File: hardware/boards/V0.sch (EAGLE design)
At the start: 140 parts, among them IC2 TPS6300, J1 SJ-43515TS-SMT, J2 HIROSE_DM3BT-DSF-PEJSHIROSE_D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, J3 MOLEX_105450-0101MOLEX_105450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, Q2 ON_SEMI_MMBT5551LT1GON_SEMI_M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, U1 VS1053-L, U2 MICROCHIP_MCP73831T-2ATI-OTMI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, X3 FH12-45S-0.5SH

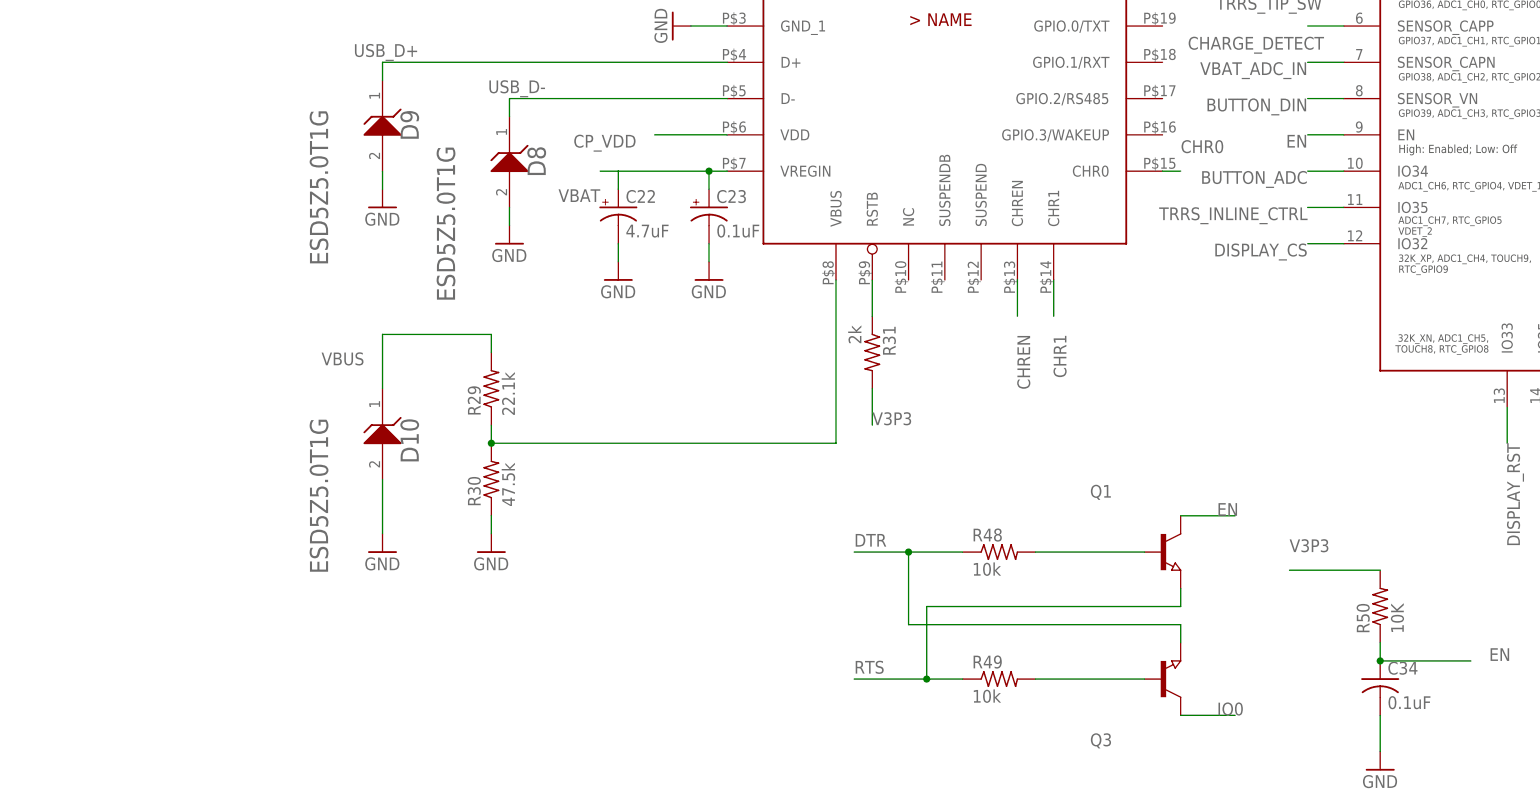
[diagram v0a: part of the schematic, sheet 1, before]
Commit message: checkpoint: swapped resistors for the esp32/cp2102N/usb port, routed the usb port, and swapped the power source for the CP2102N (runs off the 3.3V regulator now; no sense in the device appearing on computers when it isn't powered on - we'll still be able to charge though)
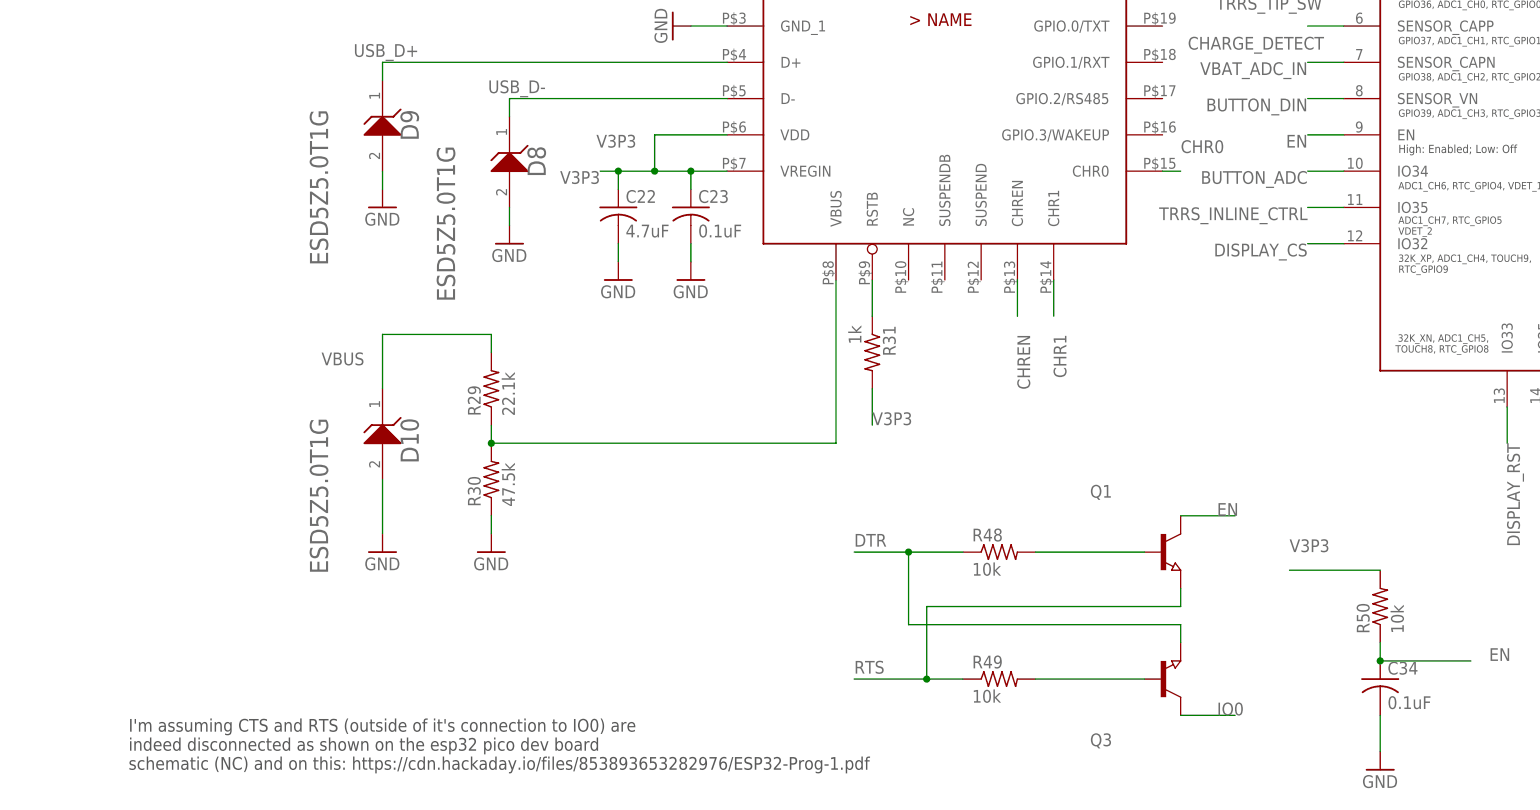
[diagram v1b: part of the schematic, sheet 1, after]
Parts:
- C22, C23: device rcl:CPOL-USC/6032-28R -> rcl:C-USC0402
- C32, C33: device rcl:C-USC1206 -> rcl:C-USC0402
- R27, R28, R29, R30, R46, R47, R48, R49: device rcl:R-US_R0805 -> rcl:R-US_R0402
- R31: value 2k -> 1k; device rcl:R-US_R0805 -> rcl:R-US_R0402
- R50: value 10K -> 10k; device rcl:R-US_R0805 -> rcl:R-US_R0402
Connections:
- net N$53 renamed CP_RSTB
- removed net CP_VDD: JL.VDD
- net GND: now also C22.2, C23.2; no longer C22.-, C23.-
- net V3P3: now also C22.1, C23.1, JL.VDD, JL.VREGIN
- net VBAT: no longer C22.+, C23.+, JL.VREGIN
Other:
- note added: "I'm assuming CTS and RTS (outside of it's connection to IO0) are indeed disconnected as shown on the esp32 pico dev board schematic (NC) and on this: https://cdn.hackaday.io/files/853893653282976/ESP32-Prog-1.pdf"

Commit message: board checkpoint
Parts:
- J12: value SJ-43515TS-SMT -> 3.5mm TRRS Jack
- renumbered J1 to J12
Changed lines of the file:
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@@
 <part name="U$5" library="CR43NP-4R7MC" deviceset="CR43NP-2R2MC" device=""/>
 <part name="BATT_CON" library="JST-S3B-XH-SM4-TB" deviceset="JST_S3B-XH-SM4-TB" device="JST_S3B-XH-SM4-TB_0_0"/>
-<part name="J1" library="TRRS-Jack-SJ-43515TS-SMT" deviceset="SJ-43515TS-SMT" device=""/>
+<part name="J12" library="TRRS-Jack-SJ-43515TS-SMT" deviceset="SJ-43515TS-SMT" device="" value="3.5mm TRRS Jack"/>
 <part name="U$6" library="AT42QT2120" deviceset="COMMS-AT42QT2120" device="XU" package3d_urn="urn:adsk.eagle:package:4349/2" value="COMMS-AT42QT2120XU"/>
 <part name="C1" library="rcl" library_urn="urn:adsk.eagle:library:334" deviceset="C-US" device="C0201" package3d_urn="urn:adsk.eagle:package:23690/2" value="50uF"/>
@@
 </plain>
 <instances>
-<instance part="J1" gate="G$1" x="111.76" y="60.96" smashed="yes" rot="R180">
+<instance part="J12" gate="G$1" x="111.76" y="60.96" smashed="yes" rot="R180">
 <attribute name="NAME" x="119.39685" y="52.55948125" size="1.78193125" layer="95" rot="R180"/>
 <attribute name="VALUE" x="119.40558125" y="71.1542" size="1.78396875" layer="96" rot="R180"/>
@@
 <net name="TRRS_TIP_SW" class="0">
 <segment>
-<pinref part="J1" gate="G$1" pin="TIP_SWITCH"/>
+<pinref part="J12" gate="G$1" pin="TIP_SWITCH"/>
 <wire x1="101.6" y1="63.5" x2="127" y2="63.5" width="0.1524" layer="91"/>
 <label x="129.54" y="63.5" size="1.778" layer="95"/>
@@
 <wire x1="96.52" y1="-5.08" x2="96.52" y2="10.16" width="0.1524" layer="91"/>
 <wire x1="96.52" y1="10.16" x2="127" y2="10.16" width="0.1524" layer="91"/>
-<pinref part="J1" gate="G$1" pin="RING2"/>
+<pinref part="J12" gate="G$1" pin="RING2"/>
 <wire x1="101.6" y1="58.42" x2="96.52" y2="58.42" width="0.1524" layer="91"/>
 <wire x1="96.52" y1="58.42" x2="96.52" y2="48.26" width="0.1524" layer="91"/>
@@
 <wire x1="20.32" y1="-2.54" x2="93.98" y2="-2.54" width="0.1524" layer="91"/>
 <wire x1="93.98" y1="-2.54" x2="93.98" y2="27.94" width="0.1524" layer="91"/>
-<pinref part="J1" gate="G$1" pin="RING1"/>
+<pinref part="J12" gate="G$1" pin="RING1"/>
 <wire x1="101.6" y1="60.96" x2="93.98" y2="60.96" width="0.1524" layer="91"/>
 <wire x1="93.98" y1="60.96" x2="93.98" y2="27.94" width="0.1524" layer="91"/>
@@
 <net name="TRRS_INLINE_CTRL" class="0">
 <segment>
-<pinref part="J1" gate="G$1" pin="SLEEVE"/>
+<pinref part="J12" gate="G$1" pin="SLEEVE"/>
 <wire x1="101.6" y1="55.88" x2="124.46" y2="55.88" width="0.1524" layer="91"/>
 <label x="129.54" y="55.88" size="1.778" layer="95"/>
@@
 <net name="N$57" class="0">
 <segment>
-<pinref part="J1" gate="G$1" pin="TIP"/>
+<pinref part="J12" gate="G$1" pin="TIP"/>
 <wire x1="91.44" y1="66.04" x2="101.6" y2="66.04" width="0.1524" layer="91"/>
 <pinref part="TP3" gate="G$1" pin="TP"/>

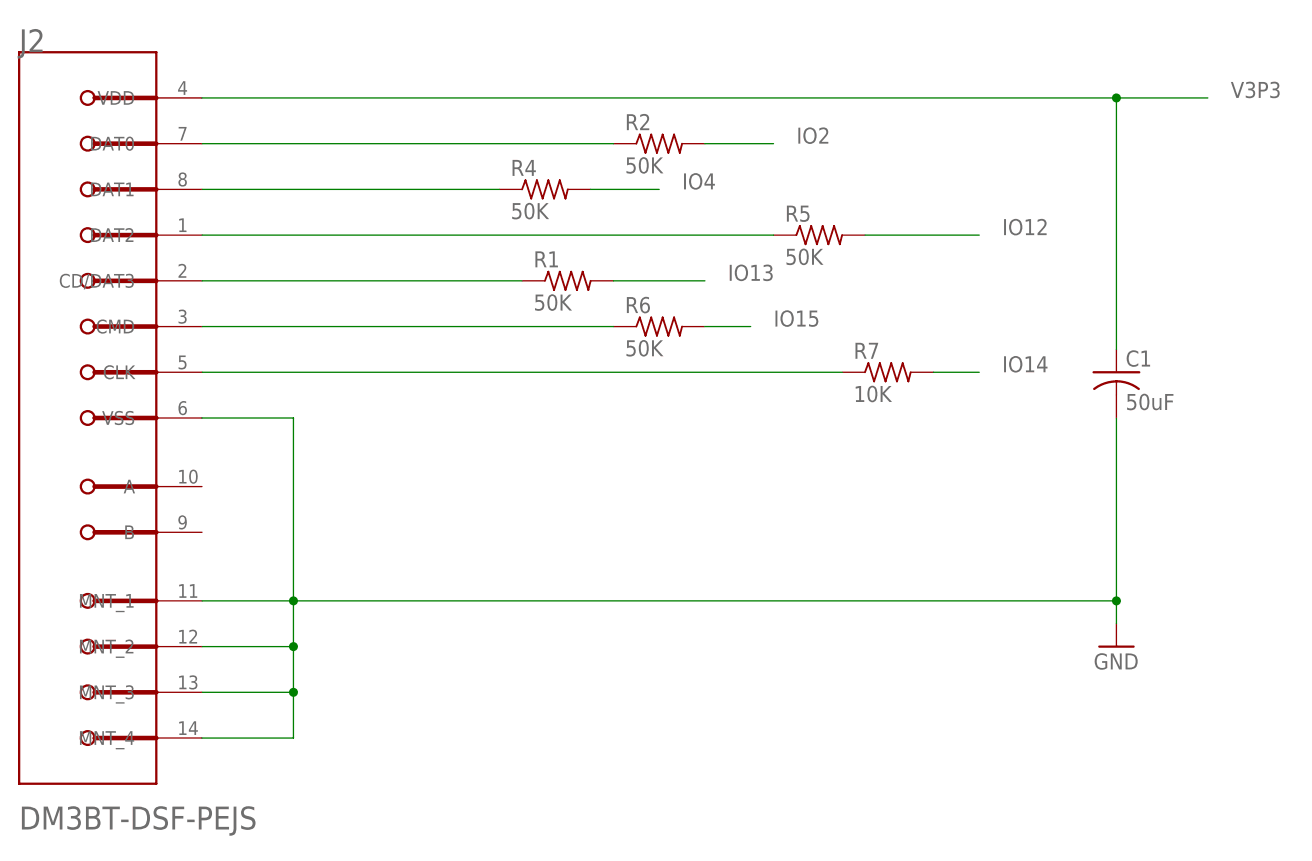
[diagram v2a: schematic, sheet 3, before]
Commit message: added pull ups to SD card
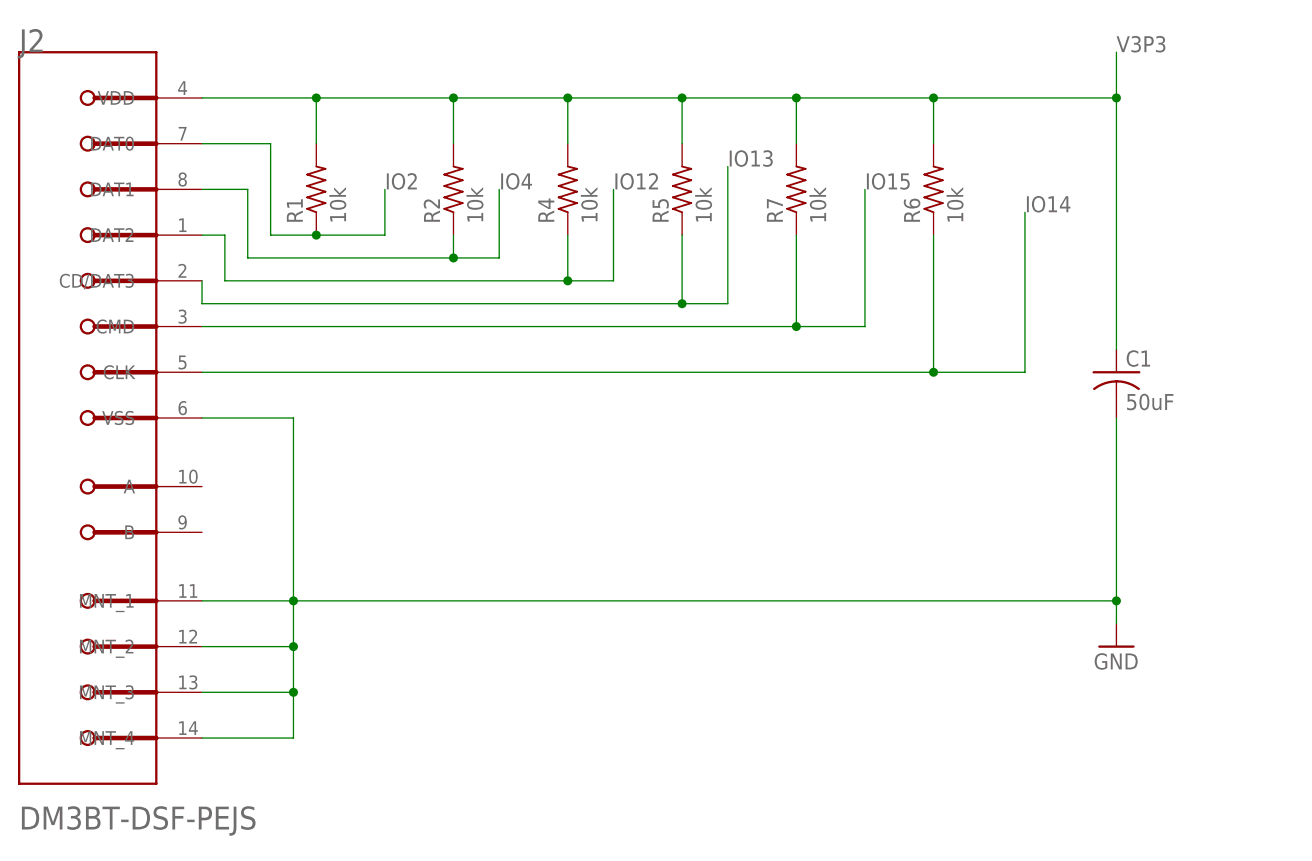
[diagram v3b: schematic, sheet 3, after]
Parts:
- R1, R2, R4, R5, R6: value 50K -> 10k
- R7: value 10K -> 10k
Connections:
- removed net N$13: J2.CD/DAT3, R1.1
- removed net N$15: J2.DAT1, R4.1
- removed net N$17: J2.DAT2, R5.1
- removed net N$2: J2.DAT0, R2.1
- removed net N$7: J2.CMD, R6.1
- removed net N$9: J2.CLK, R7.1
- net IO12: now also J2.DAT2, R4.1; no longer R5.2
- net IO13: now also J2.CD/DAT3, R5.1; no longer R1.2
- net IO14: now also J2.CLK, R6.1; no longer R7.2
- net IO15: now also J2.CMD, R7.1; no longer R6.2
- net IO2: now also J2.DAT0, R1.1; no longer R2.2
- net IO4: now also J2.DAT1, R2.1; no longer R4.2
- net V3P3: now also R1.2, R2.2, R4.2, R5.2, R6.2, R7.2
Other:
- moved on the sheet: R1, R2, R4, R5, R6, R7

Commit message: Swap resistors for the microSD Card
10k pull-ups on everything appears to work (50k does not even though some of the guides say otherwise).

Only 1-line MMC mode works so far, but there's still stuff to try.
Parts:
- C1: device rcl:C-USC0201 -> rcl:C-USC0402
- R1, R2, R4, R5, R6, R7: device adafruit:R-US_M0805 -> rcl:R-US_R0402
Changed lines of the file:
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@@
 <part name="J12" library="TRRS-Jack-SJ-43515TS-SMT" deviceset="SJ-43515TS-SMT" device="" value="3.5mm TRRS Jack"/>
 <part name="U$6" library="AT42QT2120" deviceset="COMMS-AT42QT2120" device="XU" package3d_urn="urn:adsk.eagle:package:4349/2" value="COMMS-AT42QT2120XU"/>
-<part name="C1" library="rcl" library_urn="urn:adsk.eagle:library:334" deviceset="C-US" device="C0201" package3d_urn="urn:adsk.eagle:package:23690/2" value="50uF"/>
-<part name="R1" library="adafruit" library_urn="urn:adsk.eagle:library:420" deviceset="R-US_" device="M0805" package3d_urn="urn:adsk.eagle:package:6240587/1" value="10k"/>
-<part name="R2" library="adafruit" library_urn="urn:adsk.eagle:library:420" deviceset="R-US_" device="M0805" package3d_urn="urn:adsk.eagle:package:6240587/1" value="10k"/>
-<part name="R4" library="adafruit" library_urn="urn:adsk.eagle:library:420" deviceset="R-US_" device="M0805" package3d_urn="urn:adsk.eagle:package:6240587/1" value="10k"/>
-<part name="R5" library="adafruit" library_urn="urn:adsk.eagle:library:420" deviceset="R-US_" device="M0805" package3d_urn="urn:adsk.eagle:package:6240587/1" value="10k"/>
-<part name="R6" library="adafruit" library_urn="urn:adsk.eagle:library:420" deviceset="R-US_" device="M0805" package3d_urn="urn:adsk.eagle:package:6240587/1" value="10k"/>
-<part name="R7" library="adafruit" library_urn="urn:adsk.eagle:library:420" deviceset="R-US_" device="M0805" package3d_urn="urn:adsk.eagle:package:6240587/1" value="10k"/>
+<part name="C1" library="rcl" library_urn="urn:adsk.eagle:library:334" deviceset="C-US" device="C0402" package3d_urn="urn:adsk.eagle:package:23626/2" value="50uF"/>
+<part name="R1" library="rcl" library_urn="urn:adsk.eagle:library:334" deviceset="R-US_" device="R0402" package3d_urn="urn:adsk.eagle:package:23547/3" value="10k"/>
+<part name="R2" library="rcl" library_urn="urn:adsk.eagle:library:334" deviceset="R-US_" device="R0402" package3d_urn="urn:adsk.eagle:package:23547/3" value="10k"/>
+<part name="R4" library="rcl" library_urn="urn:adsk.eagle:library:334" deviceset="R-US_" device="R0402" package3d_urn="urn:adsk.eagle:package:23547/3" value="10k"/>
+<part name="R5" library="rcl" library_urn="urn:adsk.eagle:library:334" deviceset="R-US_" device="R0402" package3d_urn="urn:adsk.eagle:package:23547/3" value="10k"/>
+<part name="R6" library="rcl" library_urn="urn:adsk.eagle:library:334" deviceset="R-US_" device="R0402" package3d_urn="urn:adsk.eagle:package:23547/3" value="10k"/>
+<part name="R7" library="rcl" library_urn="urn:adsk.eagle:library:334" deviceset="R-US_" device="R0402" package3d_urn="urn:adsk.eagle:package:23547/3" value="10k"/>
 <part name="J2" library="microSD-socket-HIROSE-DM3BT-DSF-PEJS" deviceset="HIROSE_DM3BT-DSF-PEJS" device="HIROSE_DM3BT-DSF-PEJS_0_0"/>
 <part name="R9" library="rcl" library_urn="urn:adsk.eagle:library:334" deviceset="R-US_" device="R0805" package3d_urn="urn:adsk.eagle:package:23553/2" value="100k"/>

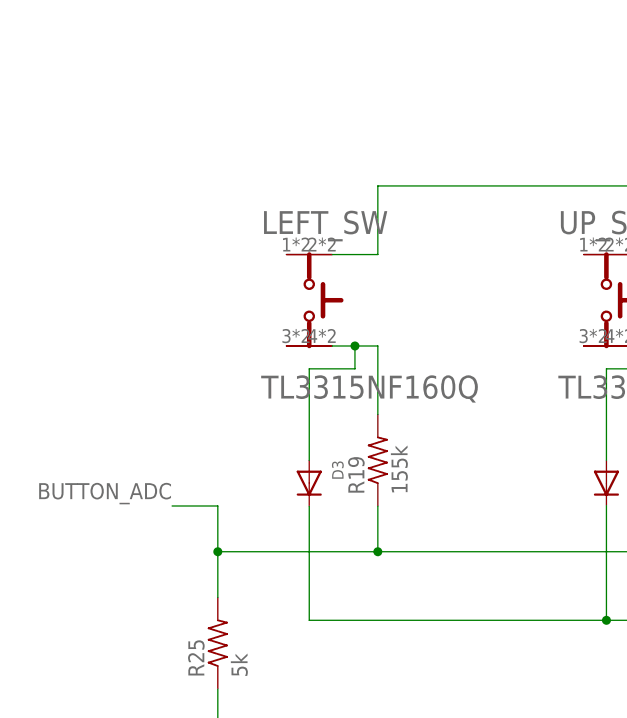
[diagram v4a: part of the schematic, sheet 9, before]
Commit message: Add an experimental card detect input to the ADC button circuit
If this is problematic we can just remove/not populate the resistor for CARD_DETECT (R54). Just adding an input to the ADC and not the full diode + digital input line too because we can just poll the ADC when we have SD card errors to make sure we've got a card in place (I'd rather not add another one of those diodes).
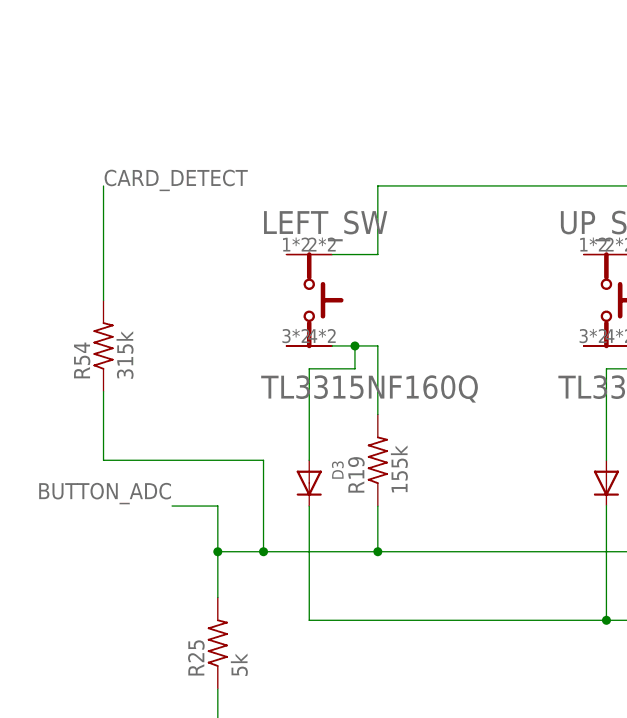
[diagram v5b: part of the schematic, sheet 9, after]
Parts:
- added R54: 315k, rcl:R-US_R0805
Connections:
- new net CARD_DETECT: J2.B, R54.2
- net BUTTON_ADC: now also R54.1
- net V3P3: now also J2.A
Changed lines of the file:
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@@
 <part name="GND48" library="supply1" library_urn="urn:adsk.eagle:library:371" deviceset="GND" device=""/>
 <part name="R53" library="rcl" library_urn="urn:adsk.eagle:library:334" deviceset="R-US_" device="R0805" package3d_urn="urn:adsk.eagle:package:23553/2" value="10k"/>
+<part name="R54" library="rcl" library_urn="urn:adsk.eagle:library:334" deviceset="R-US_" device="R0805" package3d_urn="urn:adsk.eagle:package:23553/2" value="315k"/>
 </parts>
 <sheets>
@@
 <label x="-15.24" y="101.6" size="1.778" layer="95"/>
 </segment>
+<segment>
+<pinref part="J2" gate="G$0" pin="A"/>
+<wire x1="-116.84" y1="53.34" x2="-114.3" y2="53.34" width="0.1524" layer="91"/>
+<label x="-114.3" y="53.34" size="1.778" layer="95"/>
+</segment>
 </net>
 <net name="GND" class="0">
@@
 </segment>
 </net>
+<net name="CARD_DETECT" class="0">
+<segment>
+<pinref part="J2" gate="G$0" pin="B"/>
+<wire x1="-116.84" y1="48.26" x2="-114.3" y2="48.26" width="0.1524" layer="91"/>
+<label x="-114.3" y="48.26" size="1.778" layer="95"/>
+</segment>
+</net>
 </nets>
 </sheet>
@@
 <attribute name="VALUE" x="137.16" y="5.08" size="1.778" layer="96"/>
 </instance>
+<instance part="R54" gate="G$1" x="-83.82" y="15.24" smashed="yes" rot="R90">
+<attribute name="NAME" x="-85.3186" y="11.43" size="1.778" layer="95" rot="R90"/>
+<attribute name="VALUE" x="-80.518" y="11.43" size="1.778" layer="96" rot="R90"/>
+</instance>
 </instances>
 <busses>
@@
 <wire x1="45.72" y1="-2.54" x2="45.72" y2="-7.62" width="0.1524" layer="91"/>
 <junction x="45.72" y="-7.62"/>
-<wire x1="-53.34" y1="-7.62" x2="-71.12" y2="-7.62" width="0.1524" layer="91"/>
+<wire x1="-53.34" y1="-7.62" x2="-66.04" y2="-7.62" width="0.1524" layer="91"/>
 <junction x="-53.34" y="-7.62"/>
+<wire x1="-66.04" y1="-7.62" x2="-71.12" y2="-7.62" width="0.1524" layer="91"/>
 <wire x1="-71.12" y1="-7.62" x2="-71.12" y2="-2.54" width="0.1524" layer="91"/>
 <wire x1="-71.12" y1="-2.54" x2="-76.2" y2="-2.54" width="0.1524" layer="91"/>
@@
 <wire x1="-71.12" y1="-12.7" x2="-71.12" y2="-7.62" width="0.1524" layer="91"/>
 <junction x="-71.12" y="-7.62"/>
+<wire x1="-66.04" y1="-7.62" x2="-66.04" y2="2.54" width="0.1524" layer="91"/>
+<junction x="-66.04" y="-7.62"/>
+<wire x1="-66.04" y1="2.54" x2="-83.82" y2="2.54" width="0.1524" layer="91"/>
+<wire x1="-83.82" y1="2.54" x2="-83.82" y2="10.16" width="0.1524" layer="91"/>
+<pinref part="R54" gate="G$1" pin="1"/>
 </segment>
 </net>
@@
 </segment>
 </net>
+<net name="CARD_DETECT" class="0">
+<segment>
+<pinref part="R54" gate="G$1" pin="2"/>
+<wire x1="-83.82" y1="20.32" x2="-83.82" y2="33.02" width="0.1524" layer="91"/>
+<label x="-83.82" y="33.02" size="1.778" layer="95"/>
+</segment>
+</net>
